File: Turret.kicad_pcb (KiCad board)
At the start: 2 copper layers, 104 x 54 mm, 28 parts

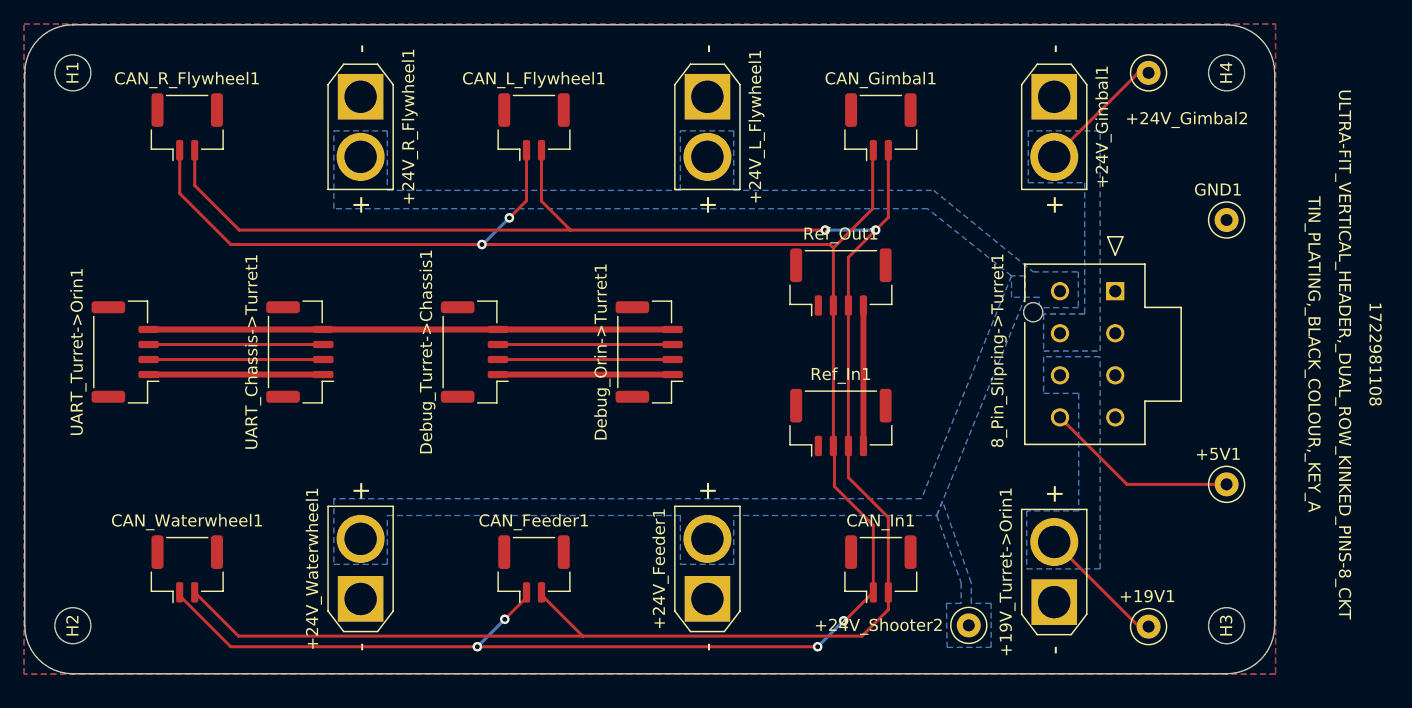
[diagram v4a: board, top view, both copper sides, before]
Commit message: New CAN Line, cleaned up schematic, changed pcb
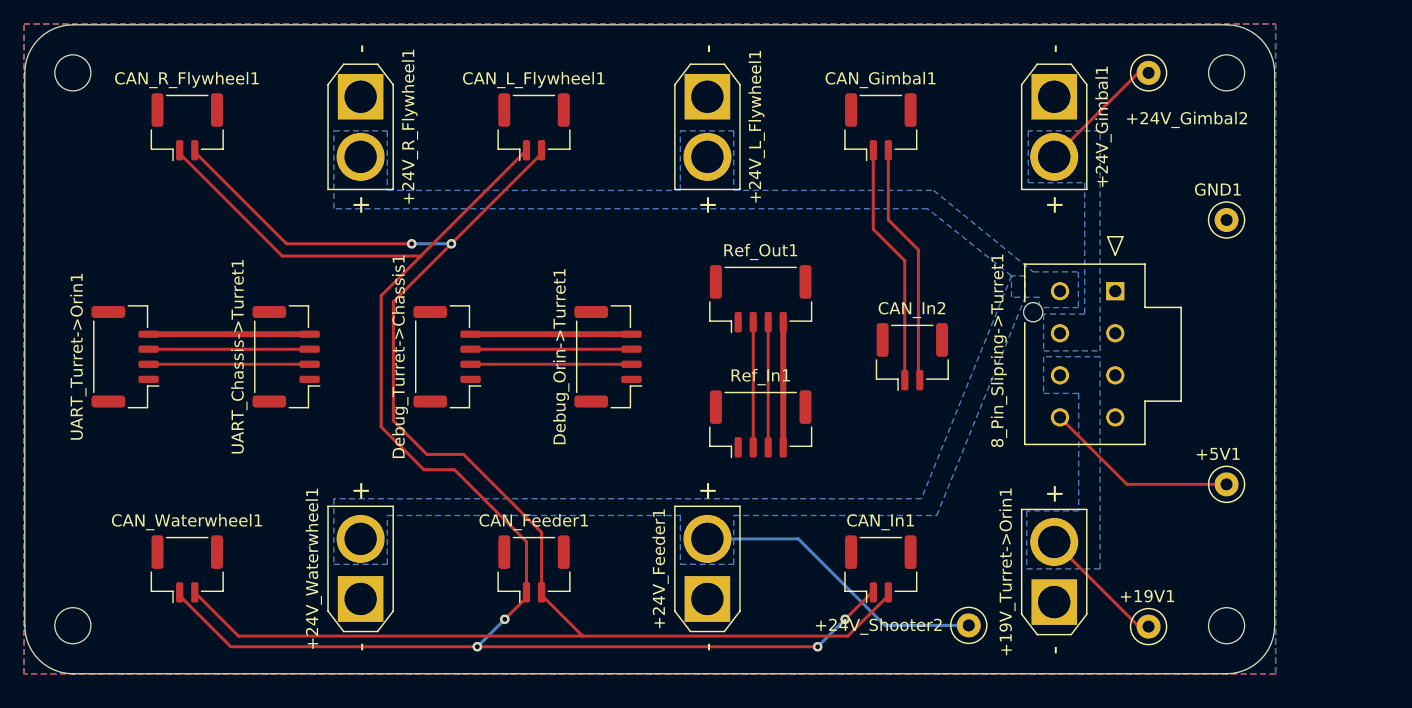
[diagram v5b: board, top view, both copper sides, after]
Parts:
- added CAN_In2: Conn_01x02_Pin, Connector_JST:JST_GH_BM02B-GHS-TBT_1x02-1MP_P1.25mm_Vertical, F.Cu at (114.3, 61.7)
- added G***: LOGO, LOGO, B.Cu at (83.6, 64.3)
- moved Ref_Out1 6.82 mm to (101.7, 56.9)
- moved Ref_In1 6.67 mm to (101.7, 67.3)
- moved Debug_Orin->Turret1 3.44 mm to (89.0, 61.7)
- moved Debug_Turret->Chassis1 2.32 mm to (75.6, 61.7)
- moved UART_Chassis->Turret1 1.21 mm to (62.2, 61.7)
- moved UART_Turret->Orin1 0.39 mm to (48.8, 61.7)
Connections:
- CAN_Gimbal1 pad 1: /CANL -> /CANLPitch
- CAN_Gimbal1 pad 2: /CANH -> /CANHPitch
- Debug_Orin->Turret1 pad 4: +3.3V -> /3.3V_Debug
- Debug_Turret->Chassis1 pad 4: +3.3V -> /3.3V_Debug
- Ref_In1 pad 2: /CANL -> /CANLRef
- Ref_In1 pad 3: /CANH -> /CANHRef
- Ref_Out1 pad 2: /CANL -> /CANLRef
- Ref_Out1 pad 3: /CANH -> /CANHRef
- UART_Chassis->Turret1 pad 4: +3.3V -> /3.3V_UART
- UART_Turret->Orin1 pad 4: +3.3V -> /3.3V_UART
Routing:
- net +3.3V: track 43.6 -> 0.00 mm
- net /CANL: track 176.7 -> 140.0 mm, vias 6 -> 4
- net /CANH: track 174.9 -> 139.4 mm
- net GND: track 29.1 -> 0.00 mm
- net /+24V_Shooter: track 0.00 -> 24.7 mm
- net /CANLPitch: track 0.00 -> 20.3 mm
- net /CANHPitch: track 0.00 -> 20.2 mm
- net /3.3V_Debug: track 0.00 -> 13.4 mm
- net /3.3V_UART: track 0.00 -> 13.4 mm
- net /CANLRef: track 0.00 -> 10.4 mm
- net /CANHRef: track 0.00 -> 10.4 mm
- net /Ref_PWR: track 11.7 -> 10.4 mm
- net /UART_TX: track 14.5 -> 13.4 mm
- net /UART_RX: track 14.5 -> 13.4 mm
- net /SWDIO: track 14.5 -> 13.4 mm
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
